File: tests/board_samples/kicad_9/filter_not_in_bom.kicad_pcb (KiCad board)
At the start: 2 copper layers, 14.2 x 16.6 mm, 4 parts

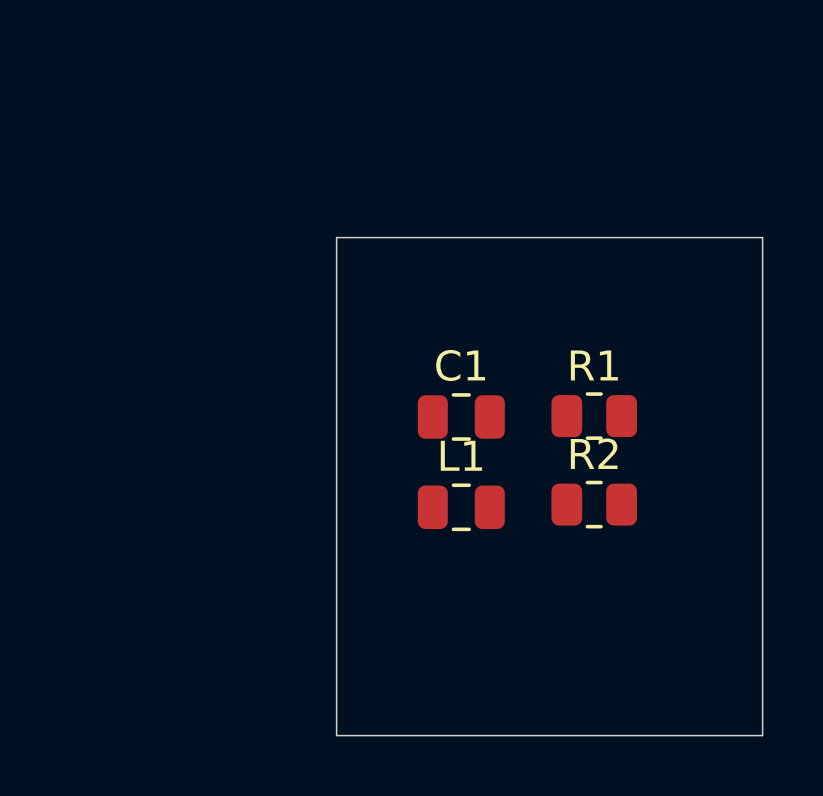
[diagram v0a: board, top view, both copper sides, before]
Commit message: [Tests][Added][KiCad 9] SCH and PCB examples
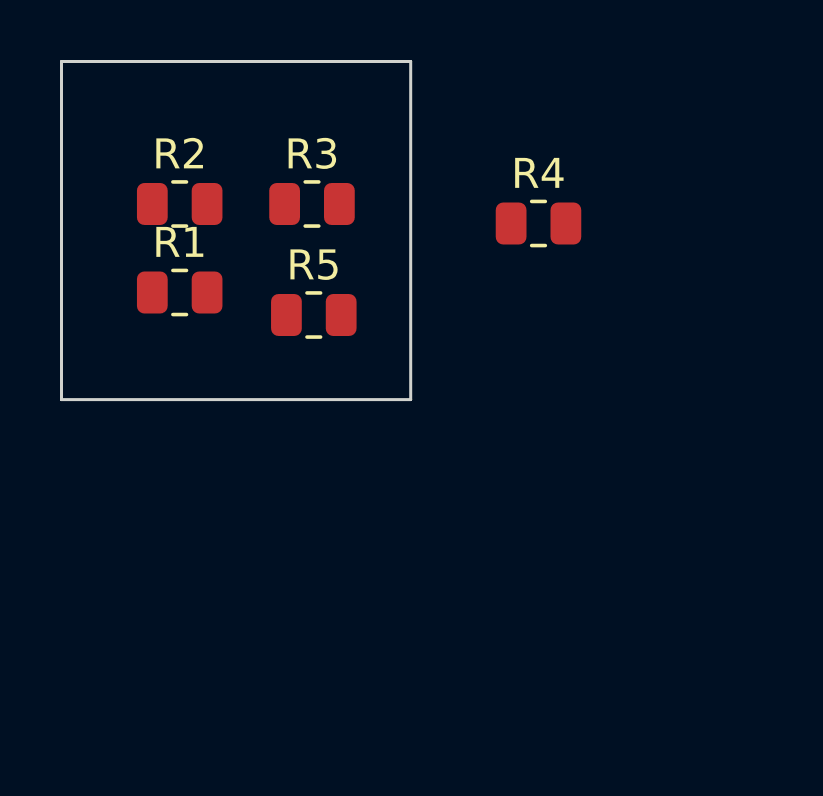
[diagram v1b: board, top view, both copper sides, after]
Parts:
- removed C1: C, Capacitor_SMD:C_0805_2012Metric
- removed L1: L, Capacitor_SMD:C_0805_2012Metric
- added R3: R, Resistor_SMD:R_0805_2012Metric, F.Cu at (125.9, 70.2)
- added R4: R, Resistor_SMD:R_0805_2012Metric, F.Cu at (133.4, 70.8)
- added R5: R, Resistor_SMD:R_0805_2012Metric, F.Cu at (125.9, 73.9)
- R2: value R_US -> R
- moved R2 17.1 mm to (121.5, 70.2)
- moved R1 14.4 mm to (121.5, 73.1)
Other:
- board size 14.2 x 16.6 mm -> 11.6 x 11.3 mm
- board text added: "Shouldn't be here Manually added The SCH says on_board='no'"
